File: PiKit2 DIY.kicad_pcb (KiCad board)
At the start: 2 copper layers, 38 parts, among them J1 Conn_01x06_Socket, J4 USB_C_Receptacle_USB2.0_16P, Q1 2N3904, Q2 2N3904, Q3 2N3906, Q4 2N3904, SW1 SW_Push, U1 PIC18F2550-ISP, X1 20Mhz

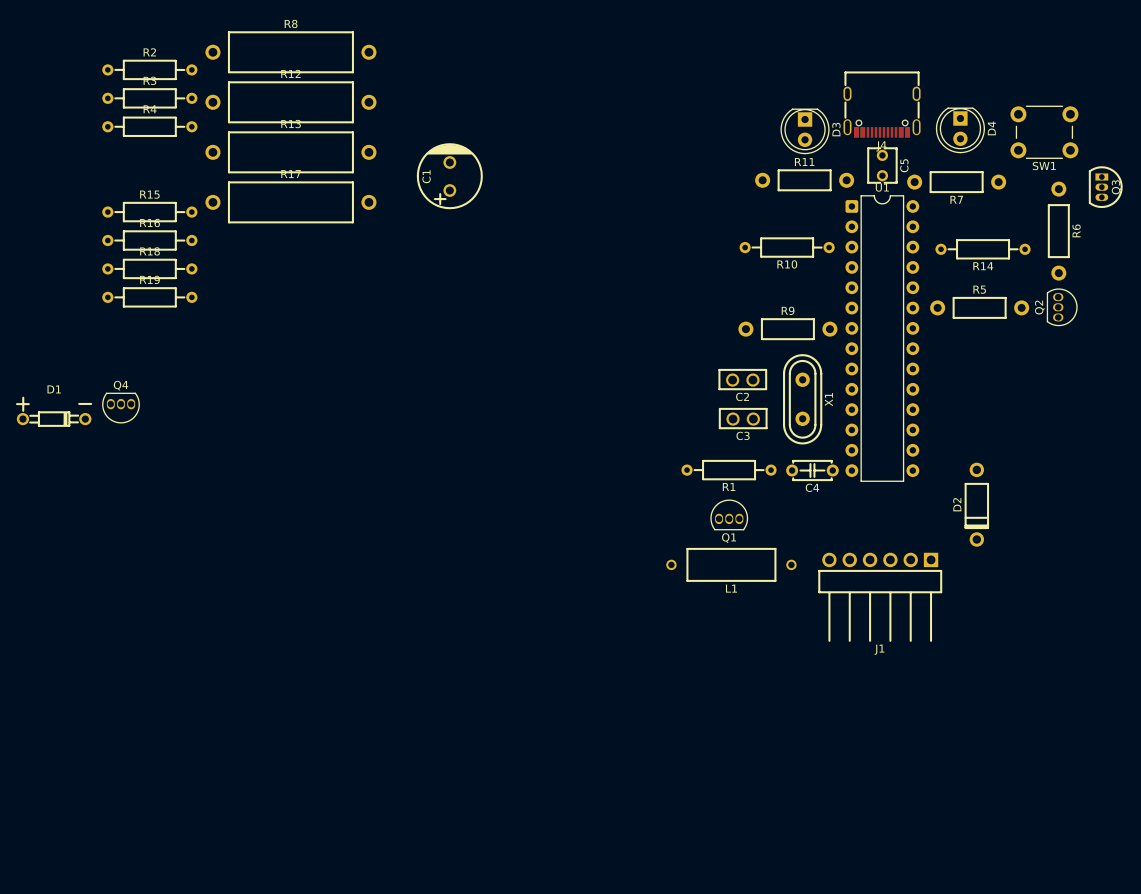
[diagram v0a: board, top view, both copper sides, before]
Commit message: Updated 100 ohm R model and footprint; Finished component placement; began routing traces
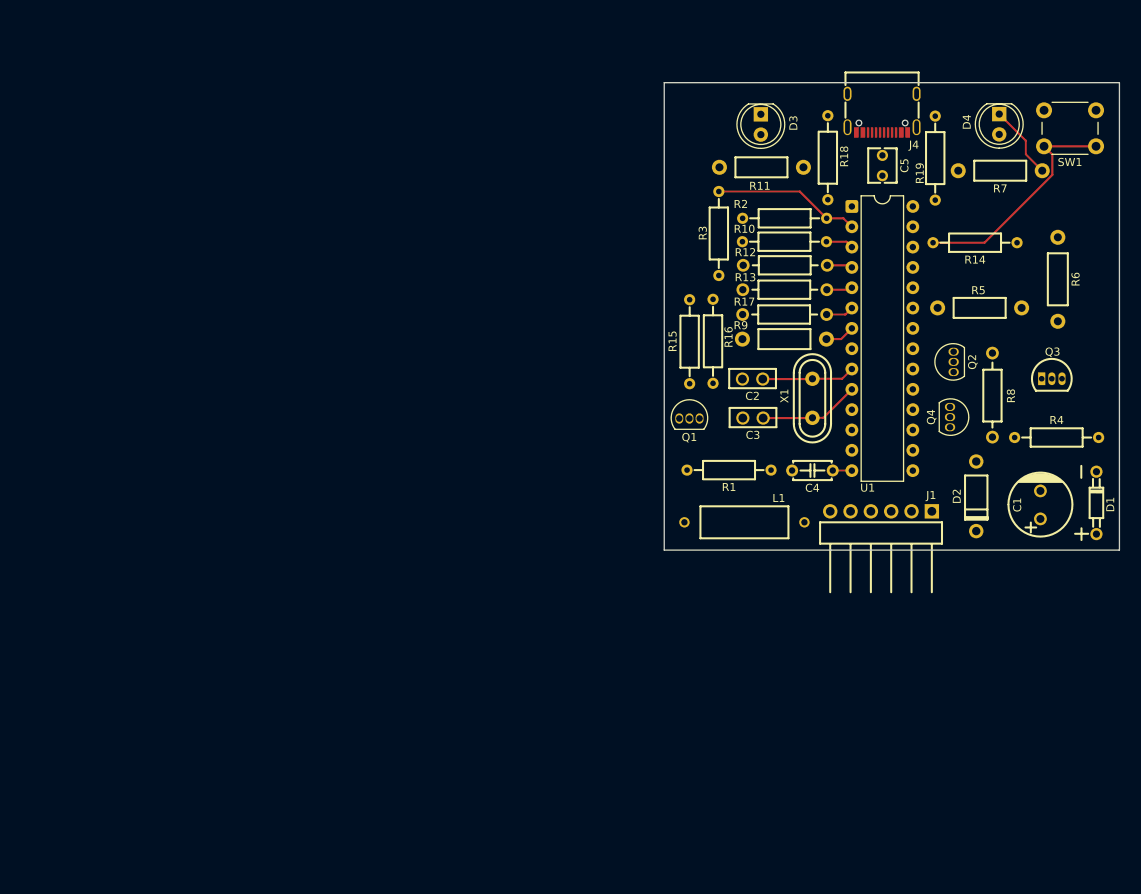
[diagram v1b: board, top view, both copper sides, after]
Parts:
- R12, R13, R17, R8: footprint JLCImport:MFR02SF1000A10 -> JLCImport:MFR0W4F1000A50
- moved D1 130.7 mm to (218.8, 79.7), turned to 90 degrees
- moved R4 119.8 mm to (213.9, 71.5)
- moved Q4 103.6 mm to (200.6, 68.9), turned to 90 degrees
- moved R19 99.7 mm to (198.7, 36.6), turned to -90 degrees
- moved R8 97.6 mm to (205.8, 66.2), turned to -90 degrees
- moved R18 85.9 mm to (185.3, 36.5), turned to 90 degrees
- moved C1 84.5 mm to (211.8, 79.9)
- moved R2 81.5 mm to (179.9, 44.1), turned to 180 degrees
- moved R3 73.1 mm to (171.7, 46.0), turned to -90 degrees
- moved R16 71.5 mm to (170.9, 59.5), turned to -90 degrees
- moved R15 69.4 mm to (168.0, 59.5), turned to 90 degrees
- moved R12 65.1 mm to (179.9, 50.0), turned to 180 degrees
- moved R13 64.1 mm to (179.9, 53.0), turned to 180 degrees
- moved R17 63.3 mm to (179.9, 56.1), turned to 180 degrees
- moved Q3 24.8 mm to (213.3, 64.2), turned to 0 degrees
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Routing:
- net 26: track 0.00 -> 28.9 mm
- net 2: track 0.00 -> 18.5 mm
- net 10: track 0.00 -> 12.6 mm
- net 9: track 0.00 -> 11.7 mm
- net Net-(D4-K): track 0.00 -> 9.30 mm
- net 7: track 0.00 -> 3.74 mm
- net 6: track 0.00 -> 3.49 mm
- net 3: track 0.00 -> 3.46 mm
- net 5: track 0.00 -> 3.23 mm
- net 4: track 0.00 -> 3.19 mm
- net 14: track 0.00 -> 2.40 mm
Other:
- board outline added: 56.9 x 58.4 mm

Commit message: KiCad: add stackup, fix nets and footprints
Add PCB stackup and layer definitions; remap many net indices and correct USB D+/D- nets and Type-C pin mappings. Adjust footprint positions, pad orientations and UUIDs, update routing (including a tuned pattern for a route), and fix silkscreen geometry. Update schematic: add D+/D- labels/wires and remove redundant global labels. Add/remove several backup zip files. These edits correct net assignments, improve component placement/orientation and refine USB routing.
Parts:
- moved J4 58.6 mm to (192.4, 89.6), turned to 0 degrees
- moved R18 49.5 mm to (199.2, 84.0), turned to -90 degrees
- moved R19 49.3 mm to (184.9, 83.9), turned to 90 degrees
- moved J1 48.6 mm to (192.0, 32.1), turned to 0 degrees
- moved C5 45.5 mm to (190.0, 83.0), turned to 90 degrees
- moved R7 2.25 mm to (204.6, 38.2)
- moved D4 2.14 mm to (204.6, 31.1)
- moved R14 1.16 mm to (204.8, 47.2), turned to 0 degrees
- moved R5 0.88 mm to (205.1, 55.3)
- moved Q4 0.84 mm to (201.4, 68.9)
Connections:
- net 15 renamed /D-
- net 16 renamed /D+
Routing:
- net +5V: track 0.00 -> 50.8 mm
- net /D+: track 0.00 -> 21.2 mm
- net /D-: track 0.00 -> 20.5 mm
- net 26: track 28.9 -> 19.5 mm
- net Net-(D4-K): track 9.30 -> 0.00 mm
- net Net-(D3-K): track 0.00 -> 8.77 mm
- net Net-(J1-Pin_4): track 0.00 -> 8.48 mm
- net Net-(J1-Pin_5): track 0.00 -> 4.22 mm
- net 23: track 0.00 -> 4.00 mm
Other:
- board size 56.9 x 58.4 mm -> 56.9 x 66.3 mm

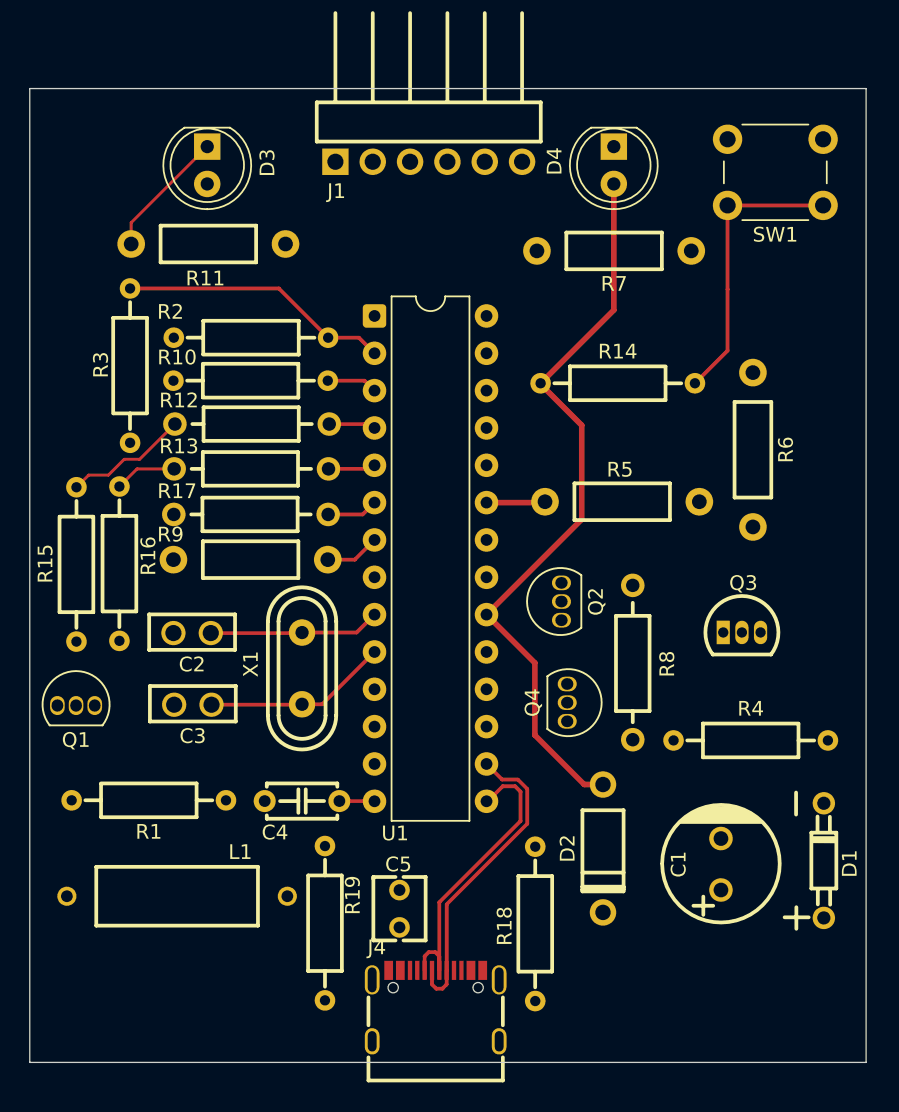
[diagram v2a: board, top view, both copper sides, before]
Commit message: Finished traces; added design rule check; added copper pours
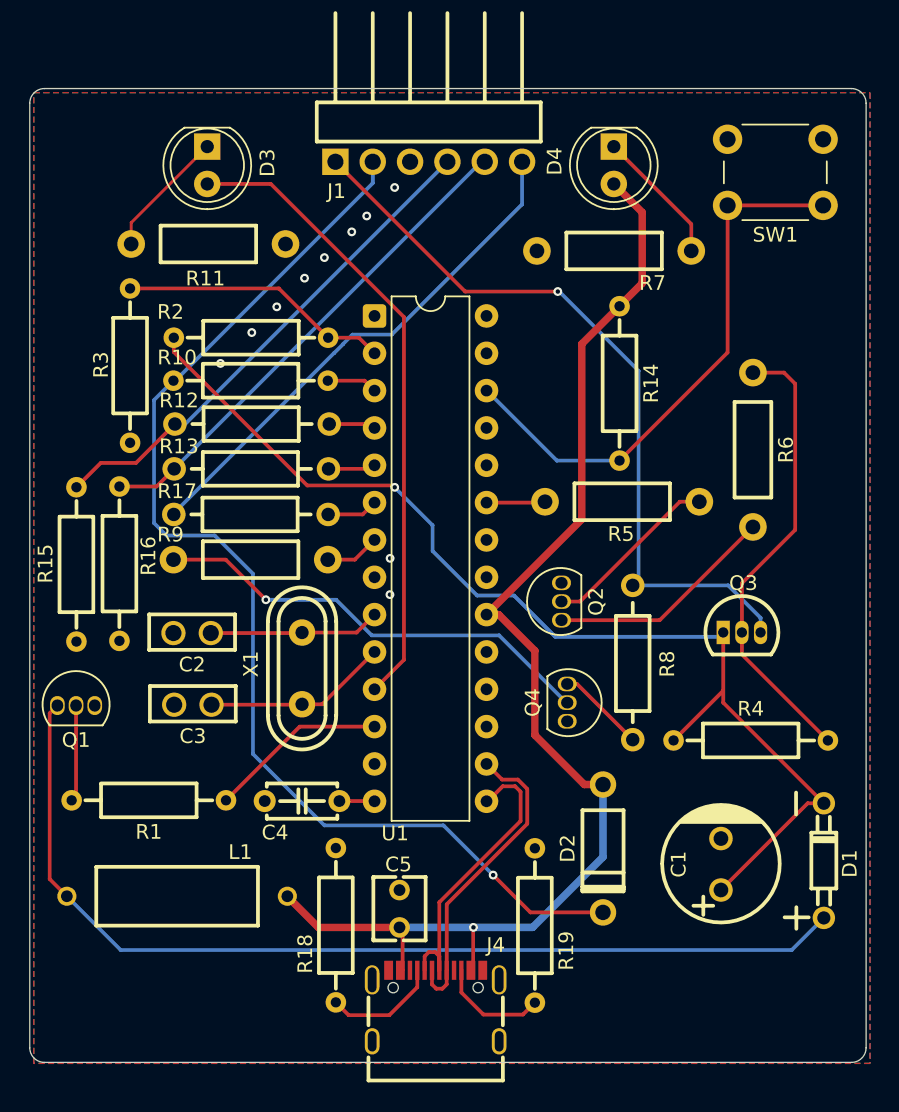
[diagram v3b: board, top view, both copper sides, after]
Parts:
- moved R19 14.3 mm to (199.2, 84.1)
- moved R18 13.6 mm to (185.7, 84.1), turned to 90 degrees
- moved R14 0.12 mm to (204.9, 47.2), turned to -90 degrees
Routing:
- net Net-(D2-K): track 0.00 -> 79.5 mm, vias 0 -> 1
- net Net-(D1-K): track 0.00 -> 76.3 mm, vias 0 -> 1
- net Net-(D1-A): track 0.00 -> 67.6 mm
- net Net-(J1-Pin_1): track 0.00 -> 51.9 mm, vias 0 -> 1
- net 11: track 0.00 -> 43.3 mm
- net +5V: track 50.8 -> 86.5 mm, vias 0 -> 1
- net Net-(J1-Pin_6): track 0.00 -> 35.4 mm
- net Net-(Q3-B): track 0.00 -> 31.4 mm
- net Net-(Q4-B): track 0.00 -> 30.9 mm, vias 0 -> 1
- net Net-(J1-Pin_5): track 4.22 -> 34.0 mm
- net Net-(J1-Pin_4): track 8.48 -> 34.4 mm
- net 26: track 19.5 -> 37.9 mm
- net Net-(Q2-C): track 0.00 -> 15.7 mm
- net Net-(Q2-B): track 0.00 -> 12.2 mm
- net 12: track 0.00 -> 12.2 mm
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- added copper zone on B.Cu, net GND
- added copper zone on F.Cu, net GND
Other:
- outline, holes or cut-outs redrawn

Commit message: Update to images
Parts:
- moved Q4 63.5 mm to (146.4, 100.7)
- moved R7 63.5 mm to (149.6, 70.0)
- moved SW1 63.5 mm to (163.8, 66.9)
- moved C2 63.5 mm to (120.9, 96.0)
- moved D3 63.5 mm to (121.9, 62.9)
- moved R1 63.5 mm to (117.9, 107.3)
- moved R13 63.5 mm to (124.9, 84.8)
- moved R3 63.5 mm to (116.7, 77.8)
- moved R16 63.5 mm to (115.9, 91.2)
- moved C1 63.5 mm to (156.9, 111.7)
- moved C3 63.5 mm to (120.9, 100.8)
- moved C4 63.5 mm to (128.4, 107.4)
- moved C5 63.5 mm to (135.0, 114.7)
- moved D1 63.5 mm to (163.9, 111.4)
- moved D2 63.5 mm to (148.8, 110.6)
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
